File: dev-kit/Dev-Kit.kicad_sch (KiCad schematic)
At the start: 0 parts

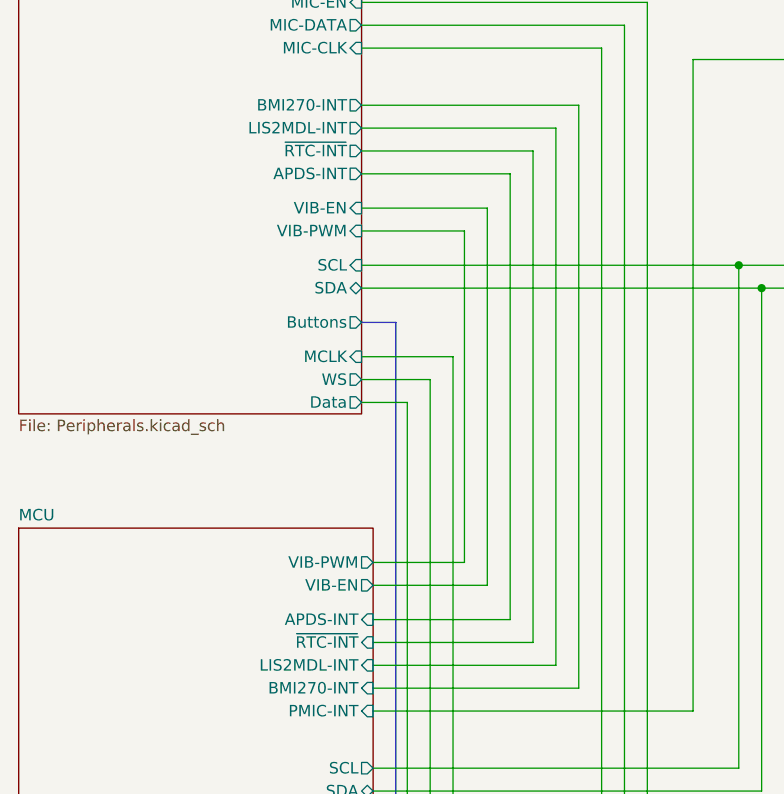
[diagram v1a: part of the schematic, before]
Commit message: Task: Issue #122
Signed-off-by: Daniel Kampert <DanielKampert@kampis-elektroecke.de>
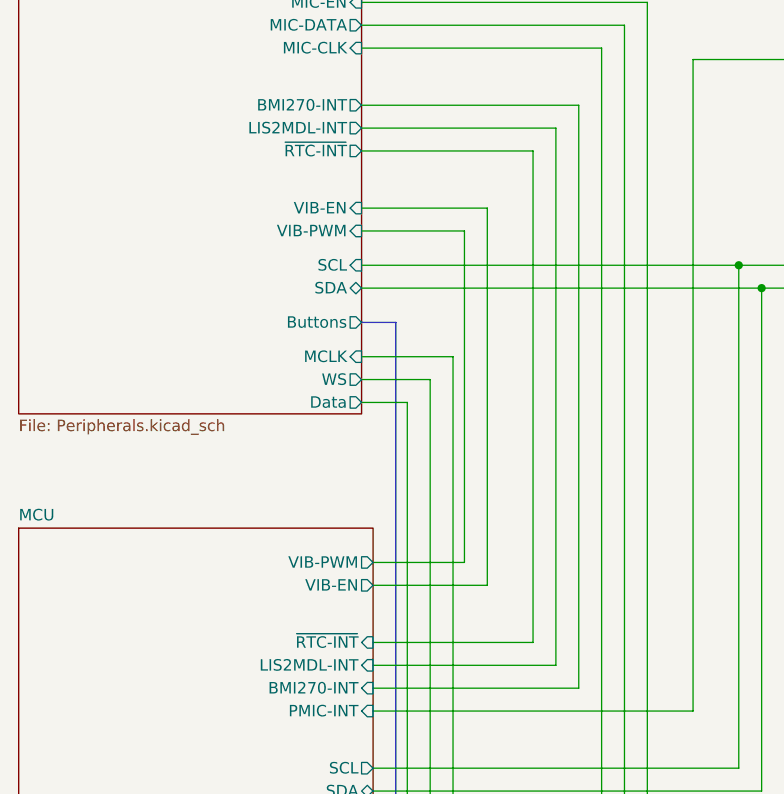
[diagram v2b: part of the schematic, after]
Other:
- sheet MCU ports: added none; removed APDS-INT
- sheet Peripherals ports: added none; removed APDS-INT
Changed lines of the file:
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@@
-	(wire
-		(pts
-			(xy 81.28 57.15) (xy 81.28 106.68)
-		)
-		(stroke
-			(width 0)
-			(type default)
-		)
-	)
 	(wire
 		(pts
@@
 	(wire
 		(pts
-			(xy 81.28 106.68) (xy 66.04 106.68)
-		)
-		(stroke
-			(width 0)
-			(type default)
-		)
-	)
-	(wire
-		(pts
 			(xy 78.74 60.96) (xy 78.74 102.87)
 		)
@@
 		(pts
 			(xy 64.77 80.01) (xy 72.39 80.01)
-		)
-		(stroke
-			(width 0)
-			(type default)
-		)
-	)
-	(wire
-		(pts
-			(xy 64.77 57.15) (xy 81.28 57.15)
 		)
 		(stroke
@@
 			)
 		)
-		(pin "APDS-INT" output
-			(at 64.77 57.15 0)
-			(effects
-				(font
-					(size 1.27 1.27)
-				)
-				(justify right)
-			)
-		)
 		(pin "VIB-EN" input
 			(at 64.77 60.96 0)
@@
 			(effects
 				(font
-					(size 1.27 1.27)
-				)
-				(justify right)
-			)
-		)
-		(pin "APDS-INT" input
-			(at 66.04 106.68 0)
-			(effects
-				(font
